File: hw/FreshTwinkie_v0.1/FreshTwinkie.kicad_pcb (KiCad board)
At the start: 2 copper layers, 32.8 x 35.5 mm, 54 parts, among them J1 USB_C_Receptacle, J2 USB_B_Micro, P1 USB_C_Plug, Q1 BSD84, Q2 BSD84, Q3 BSD84, Q4 BSD84, SW1 SW_Push, U1 AD8606ARMZ-REEL, U2 STM32F072CBUx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

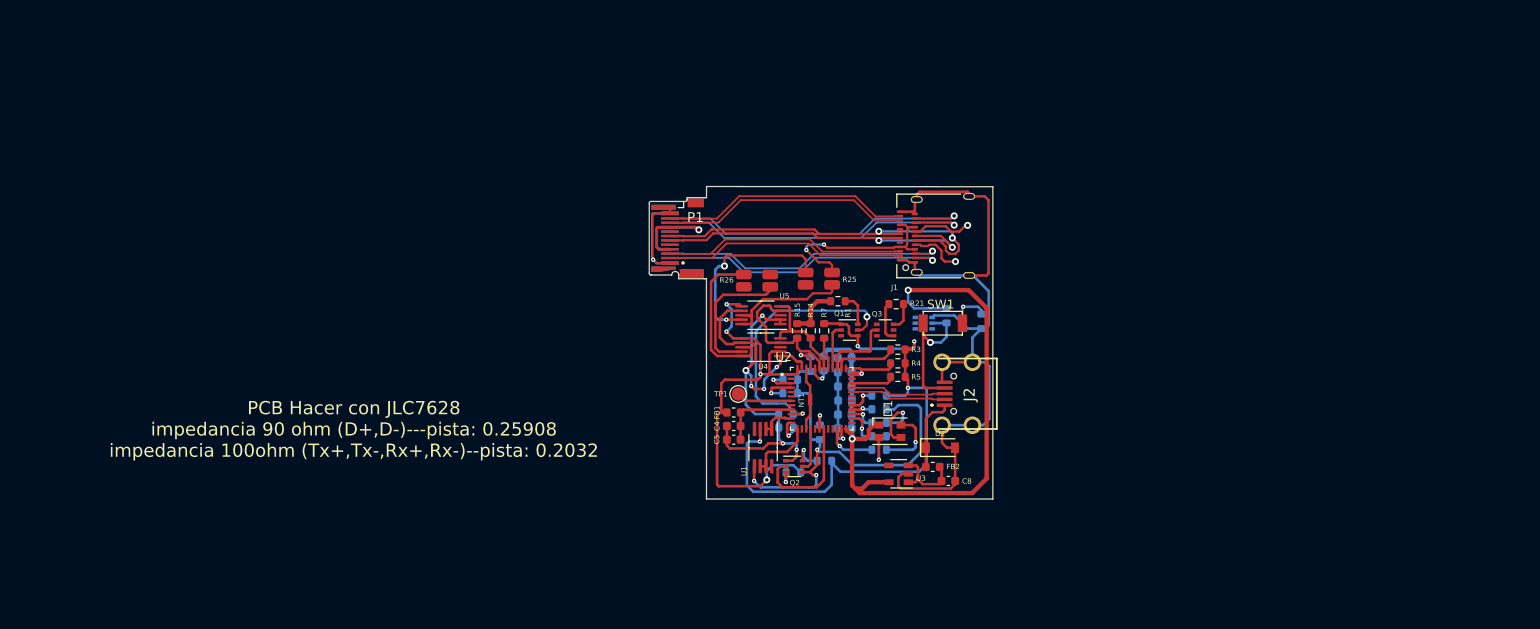
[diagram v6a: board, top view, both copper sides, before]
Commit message: routingRShunttoUSBC
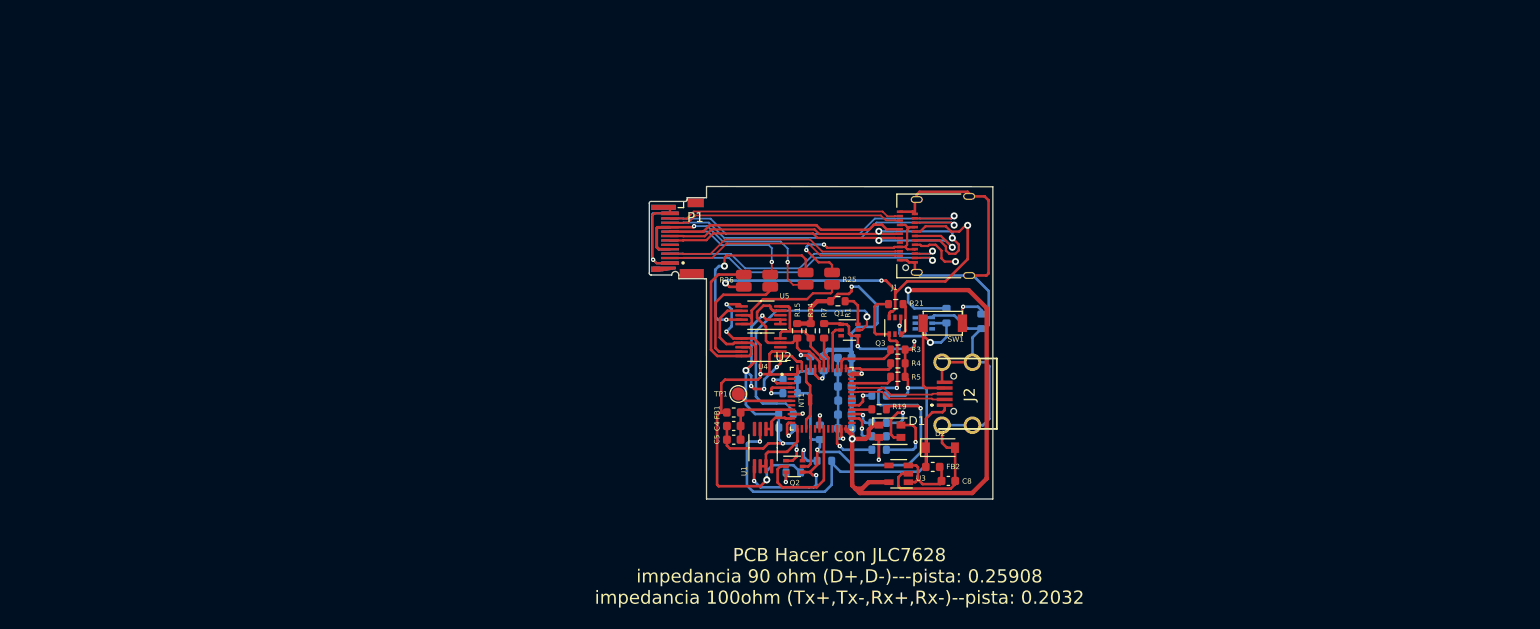
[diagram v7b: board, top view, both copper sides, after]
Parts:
- R19: moved to F.Cu
- moved Q3 1.21 mm to (157.5, 105.9), turned to 90 degrees
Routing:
- net /USBC_CC2: track 6.78 -> 46.0 mm, vias 1 -> 3
- net /USB_C_SBU1: track 0.00 -> 27.1 mm
- net /CC2: track 54.2 -> 71.5 mm, vias 3 -> 5
- net Net-(P1-PadA4): track 17.4 -> 33.6 mm, vias 1 -> 2
- net +3V3: track 139.4 -> 154.8 mm, vias 7 -> 8
- net Net-(P1-PadB5): track 0.00 -> 15.4 mm, vias 0 -> 1
- net /CC2_TX_EN: track 8.46 -> 0.00 mm
- net GND: track 177.9 -> 185.5 mm, vias 9 -> 10
- net /RX2+: track 28.1 -> 26.7 mm
- net /RX2-: track 28.1 -> 26.7 mm
- net Net-(Q3-Pad3): track 3.16 -> 3.84 mm
- net /CC2_RA: track 2.38 -> 2.28 mm, vias 1 -> 0

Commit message: routeFinished
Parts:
- moved NT1 1.56 mm to (148.6, 112.9), turned to 180 degrees
- moved R3 0.30 mm to (157.6, 108.6)
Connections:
- P1 pad S3: (no net) -> GND
- P1 pad S4: (no net) -> GND
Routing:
- net GND: track 185.5 -> 270.4 mm, vias 10 -> 15
- net /BOOT: track 2.62 -> 65.8 mm, vias 1 -> 5
- net /CC2_EN: track 3.09 -> 54.3 mm, vias 1 -> 5
- net /VBUS_ALERT_L: track 0.00 -> 47.2 mm, vias 0 -> 4
- net /USBC_CC1: track 0.00 -> 45.8 mm, vias 0 -> 3
- net /USB_C_SBU2: track 6.04 -> 35.3 mm, vias 1 -> 3
- net /CC2_ALERT_L: track 0.00 -> 14.7 mm, vias 0 -> 3
- net /CC2_TX_EN: track 0.00 -> 12.7 mm, vias 0 -> 6
- net +3V3: track 154.8 -> 162.9 mm, vias 8 -> 9
- net Net-(J1-PadA4): track 22.4 -> 16.6 mm
- net /USBC_D-: track 43.6 -> 38.6 mm
- net /USBC_D+: track 40.3 -> 35.5 mm
- net /CC2: track 71.5 -> 67.2 mm
- net /RX1-: track 33.4 -> 37.4 mm
- net /RX1+: track 33.4 -> 37.4 mm
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- added copper zone on B.Cu, net GND
- added copper zone on F.Cu, net GND
